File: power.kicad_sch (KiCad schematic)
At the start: 13 parts, among them U16 power_conn_10, U17 REF191, U18 L78L05ACU, U19 ZLDO1117G33TA, U20 TL072

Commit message: working on the PCB
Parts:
- removed C17: C-Pol-10uF-FK-V, Capacitor_SMD:CP_Elec_8x6.2, symbol eurorack:C-Pol-10uF-FK-V
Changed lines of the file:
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@@
   (junction (at 109.855 75.565) (diameter 0) (color 0 0 0 0)
   )
-  (junction (at 33.02 91.44) (diameter 0) (color 0 0 0 0)
-  )
   (junction (at 57.785 92.71) (diameter 0) (color 0 0 0 0)
   )
@@
     (stroke (width 0) (type default) (color 0 0 0 0))
   )
-  (wire (pts (xy 33.02 91.44) (xy 46.99 91.44))
+  (wire (pts (xy 27.305 91.44) (xy 46.99 91.44))
     (stroke (width 0) (type default) (color 0 0 0 0))
   )
@@
   )
   (wire (pts (xy 143.51 43.18) (xy 143.51 39.37))
-    (stroke (width 0) (type default) (color 0 0 0 0))
-  )
-  (wire (pts (xy 27.305 91.44) (xy 33.02 91.44))
     (stroke (width 0) (type default) (color 0 0 0 0))
   )
@@
       (effects (font (size 1.27 1.27)) hide)
     )
-    (pin "1")
-    (pin "2")
-  )
-  (symbol (lib_id "eurorack:C-Pol-10uF-FK-V") (at 33.02 87.63 0) (unit 1)
-    (in_bom yes) (on_board yes)
-    (property "Reference" "C17" (id 0) (at 33.655 85.725 0)
-      (effects (font (size 1.27 1.27)) (justify left))
-    )
-    (property "Value" "C-Pol-10uF-FK-V" (id 1) (at 23.495 95.25 0)
-      (effects (font (size 1.27 1.27)) (justify left))
-    )
-    (property "Footprint" "Capacitor_SMD:CP_Elec_8x6.2" (id 2) (at 33.9852 91.44 0)
-      (effects (font (size 1.27 1.27)) hide)
-    )
-    (property "Datasheet" "https://secure.reichelt.com/at/en/e-cap-smd-10-uf-16-v-105-c-2000-h-low-esr-fk-v-10u-16-p200127.html?&trstct=pos_6&nbc=1" (id 3) (at 33.02 87.63 0)
-      (effects (font (size 1.27 1.27)) hide)
-    )

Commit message: reworking with Pot Lights
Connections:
- net +12V: now also U18.3 (IN); no longer U18.1 (IN)
- net +5V: now also U18.1 (OUT); no longer U18.3 (OUT)
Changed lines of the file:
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@@
       (effects (font (size 1.27 1.27)) hide)
     )
-    (property "Datasheet" "https://www.reichelt.com/at/en/ldo-voltage-regulator-3-3v-sot-223-3-zldo1117g33ta-p219149.html?&trstct=pos_13&nbc=1" (id 3) (at 92.075 58.42 0)
+    (property "Datasheet" "https://www.reichelt.at/at/en/ldo-voltage-regulator-3-3v-sot-223-3-zldo1117g33ta-p219149.html?&trstct=pos_13&nbc=1" (id 3) (at 92.075 58.42 0)
       (effects (font (size 1.27 1.27)) hide)
     )

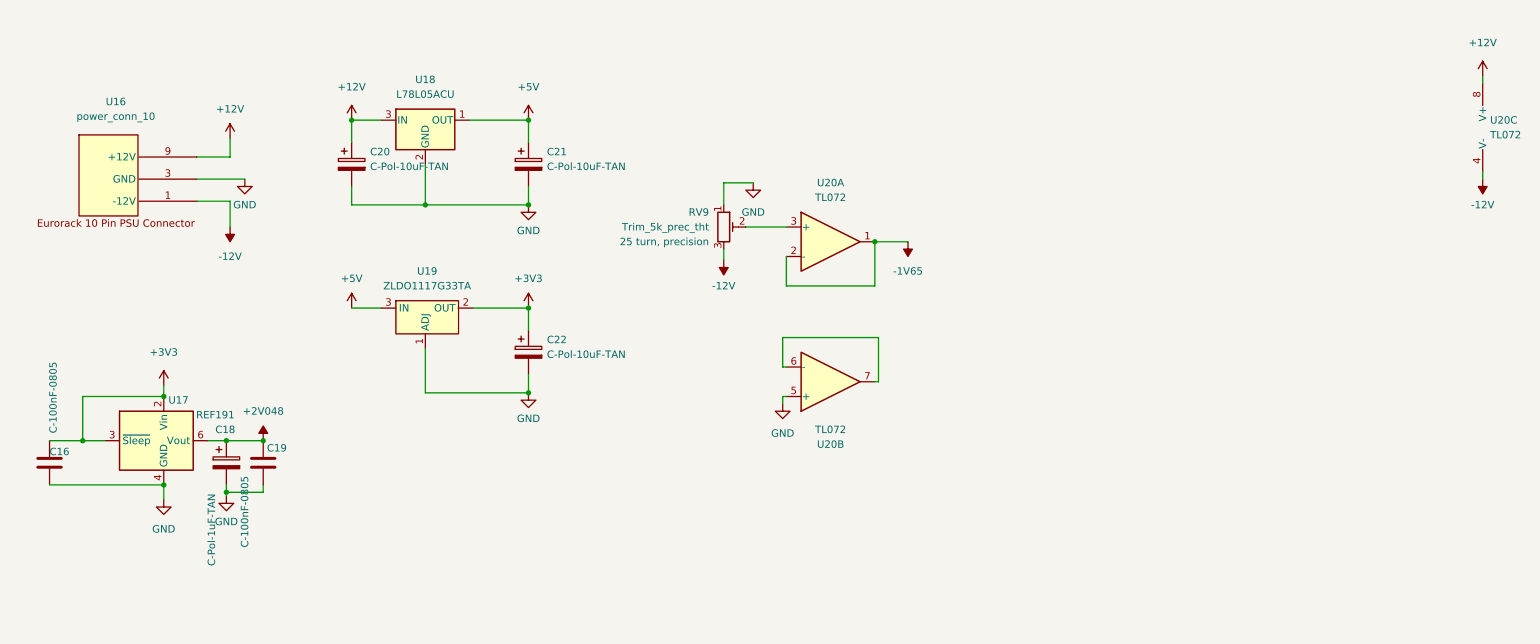
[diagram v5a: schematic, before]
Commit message: fixed issues, power still needs to be addressed
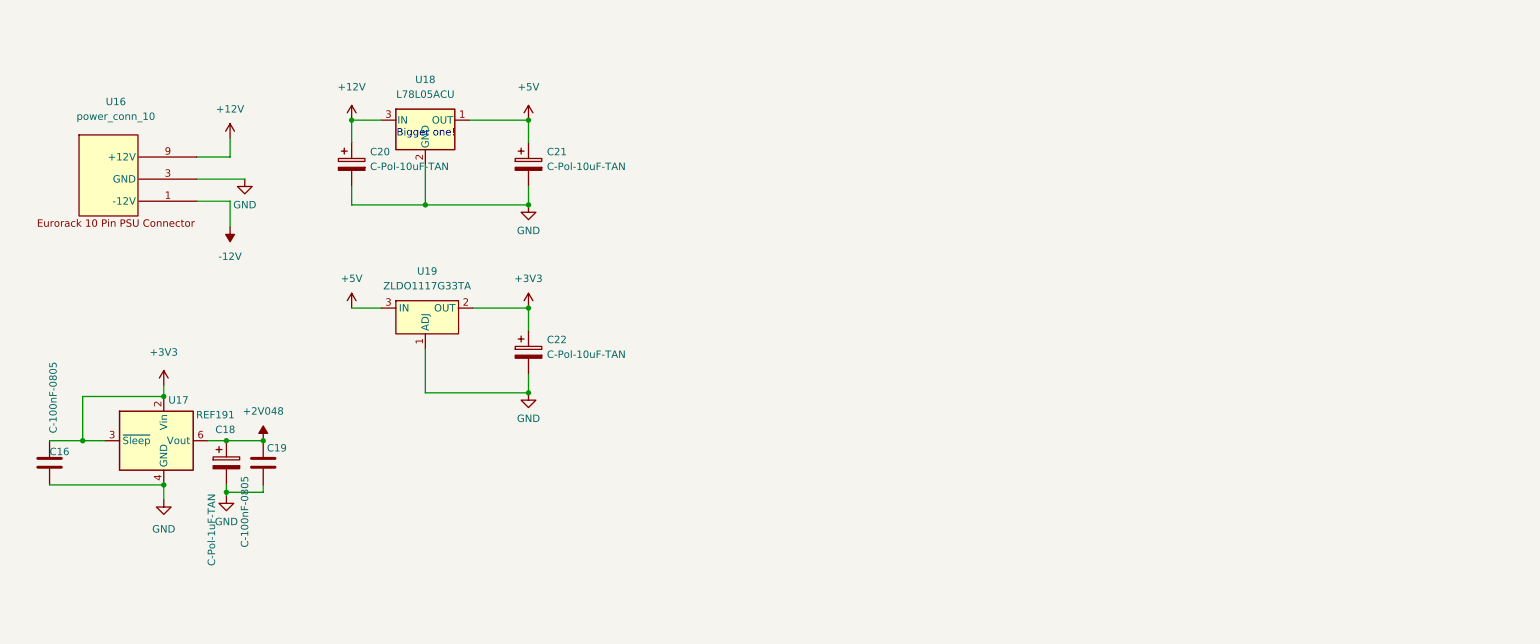
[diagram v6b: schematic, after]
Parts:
- removed RV9: Trim_5k_prec_tht, eurorack:trim_2.5mm, symbol eurorack:Trim_5k_prec_tht
- removed U20: TL072, Package_SO:SO-8_3.9x4.9mm_P1.27mm, symbol eurorack:TL072
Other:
- note added: "Bigger one!"

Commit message: New design
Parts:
- removed U16: power_conn_10, eurorack:power_10, symbol eurorack:power_conn_10
- removed U18: L78L05ACU, Package_TO_SOT_SMD:SOT-89-3_Handsoldering, symbol eurorack:L78L05ACU
- added C24, C25: C-Pol-10uF-TAN, Capacitor_Tantalum_SMD:CP_EIA-6032-28_Kemet-C, symbol eurorack:C-Pol-10uF-TAN
- added JP2: Jumper_2_Open, Jumper:SolderJumper-2_P1.3mm_Open_Pad1.0x1.5mm, symbol Jumper:Jumper_2_Open
- added U16: power_conn_16, eurorack:power_16, symbol eurorack:power_conn_16
- added U18: LM7805_TO220, Package_TO_SOT_THT:TO-220-3_Vertical, symbol Regulator_Linear:LM7805_TO220
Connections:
- net +12V: now also C24.1, U16.10 (+12V), U16.9 (+12V), U18.1 (VI)
- net +5V: now also JP2.2 (B), U16.11 (+5V), U16.12 (+5V)
- net -12V: now also C25.2, U16.1 (-12V), U16.2 (-12V)
- net GND: now also C24.2, C25.1, U16.3 (GND), U16.4 (GND), U16.5 (GND), U16.6 (GND), U16.7 (GND), U16.8 (GND), U18.2 (GND)
- new net: U16.13 (CV), U16.14 (CV)
- new net: U16.15 (GATE), U16.16 (GATE)
- new net: JP2.1 (A), U18.3 (VO)
- no-connect marks 0 -> 2
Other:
- note removed: "Bigger one!"

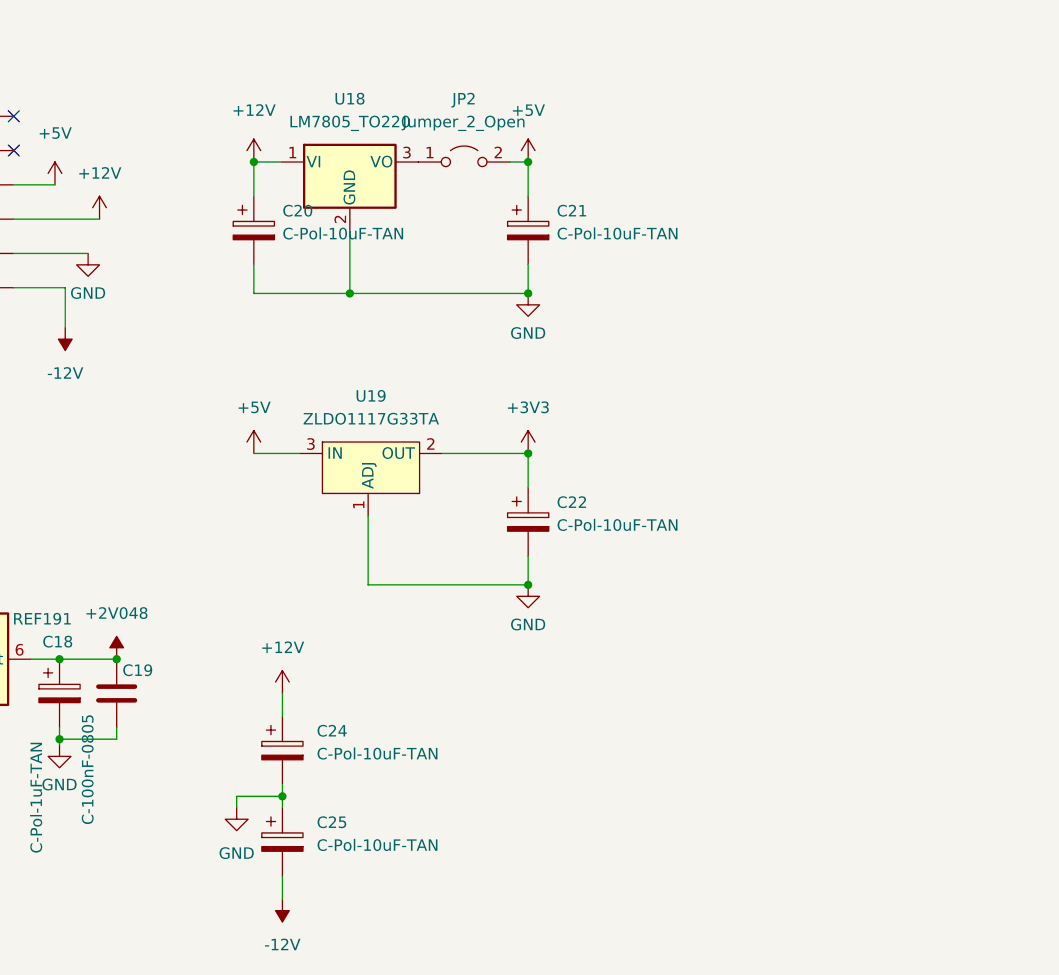
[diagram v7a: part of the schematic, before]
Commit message: working on lifted leds
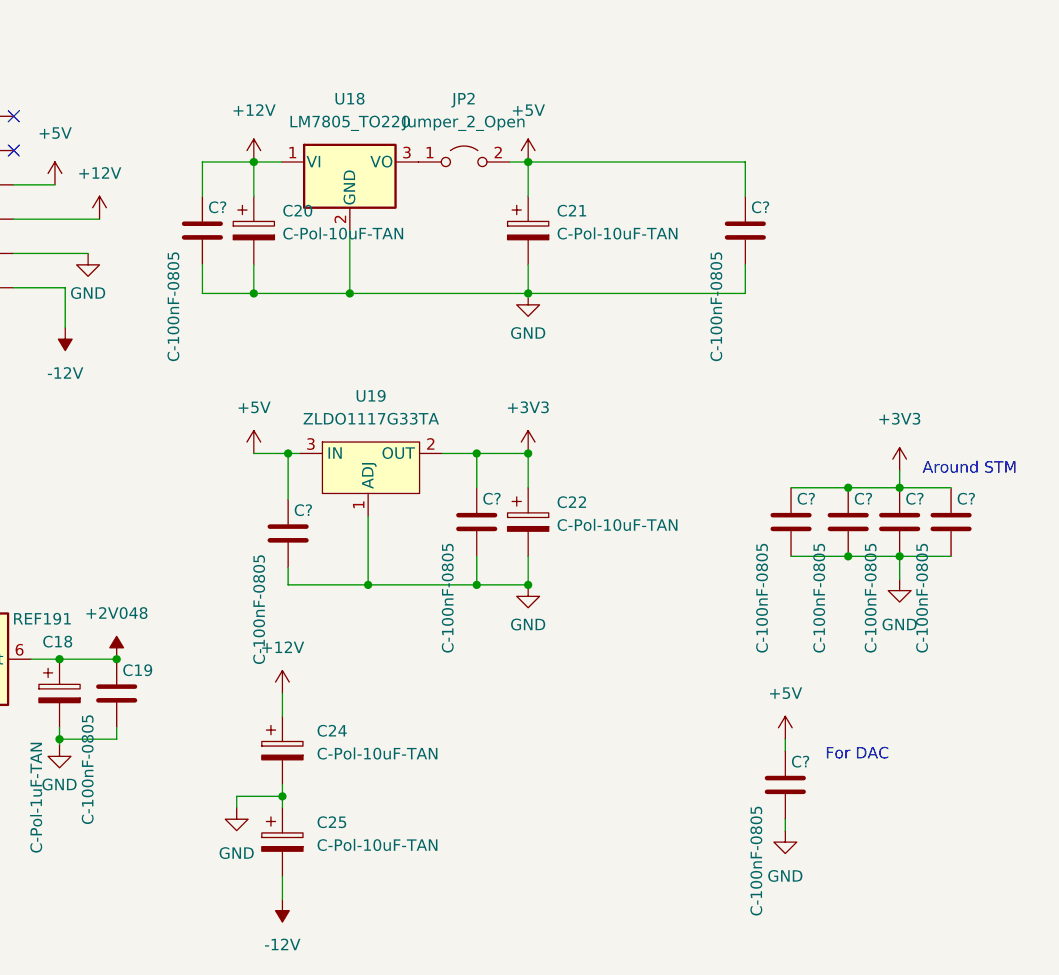
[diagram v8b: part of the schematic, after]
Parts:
- added C? (x9): C-100nF-0805, Capacitor_SMD:C_0805_2012Metric_Pad1.18x1.45mm_HandSolder, symbol eurorack:C-100nF-0805
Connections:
- net +12V: now also C?.1
- net +3V3: now also C?.1, C?.1, C?.1, C?.1, C?.1
- net +5V: now also C?.1, C?.1, C?.1
- net GND: now also C?.2, C?.2, C?.2, C?.2, C?.2, C?.2, C?.2, C?.2, C?.2
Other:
- note added: "Around STM"
- note added: "For DAC"
